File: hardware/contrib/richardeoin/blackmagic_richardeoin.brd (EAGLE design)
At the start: 5 parts, among them Q2 IRLML5103

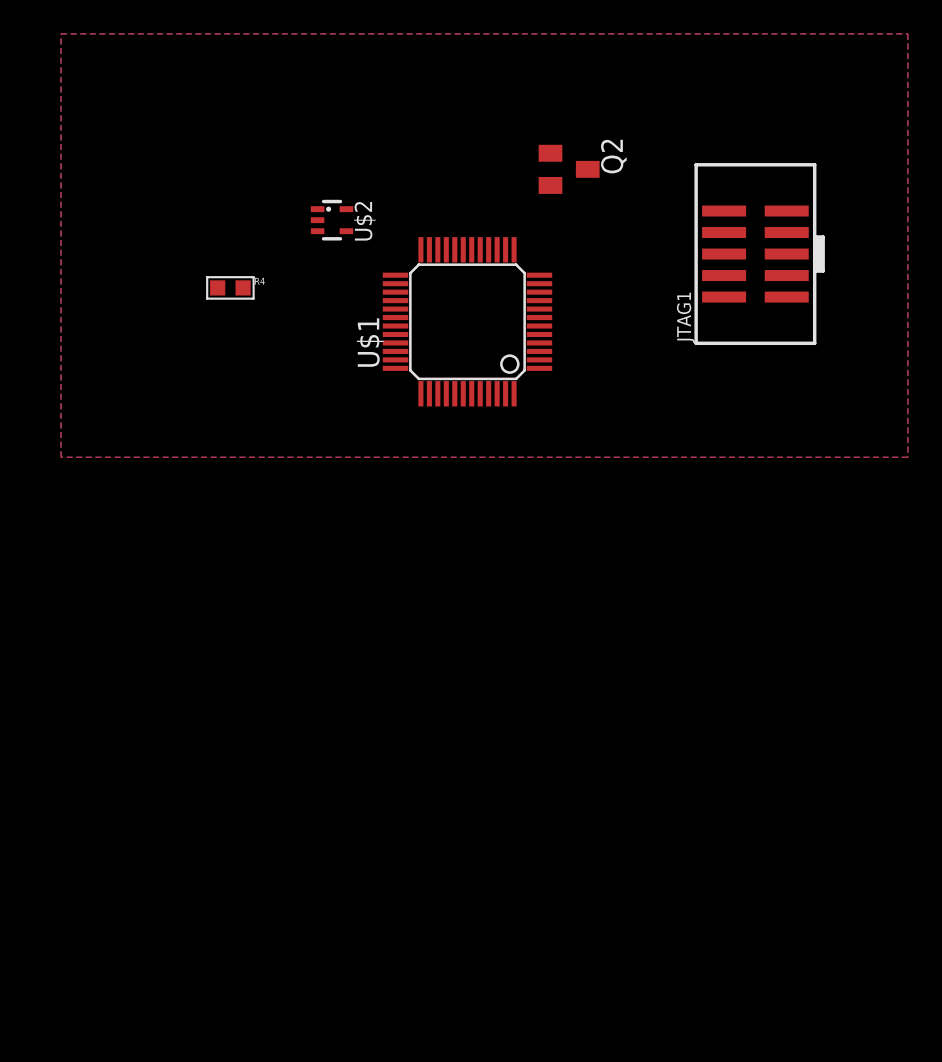
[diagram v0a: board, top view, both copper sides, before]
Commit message: Majority of Components in place
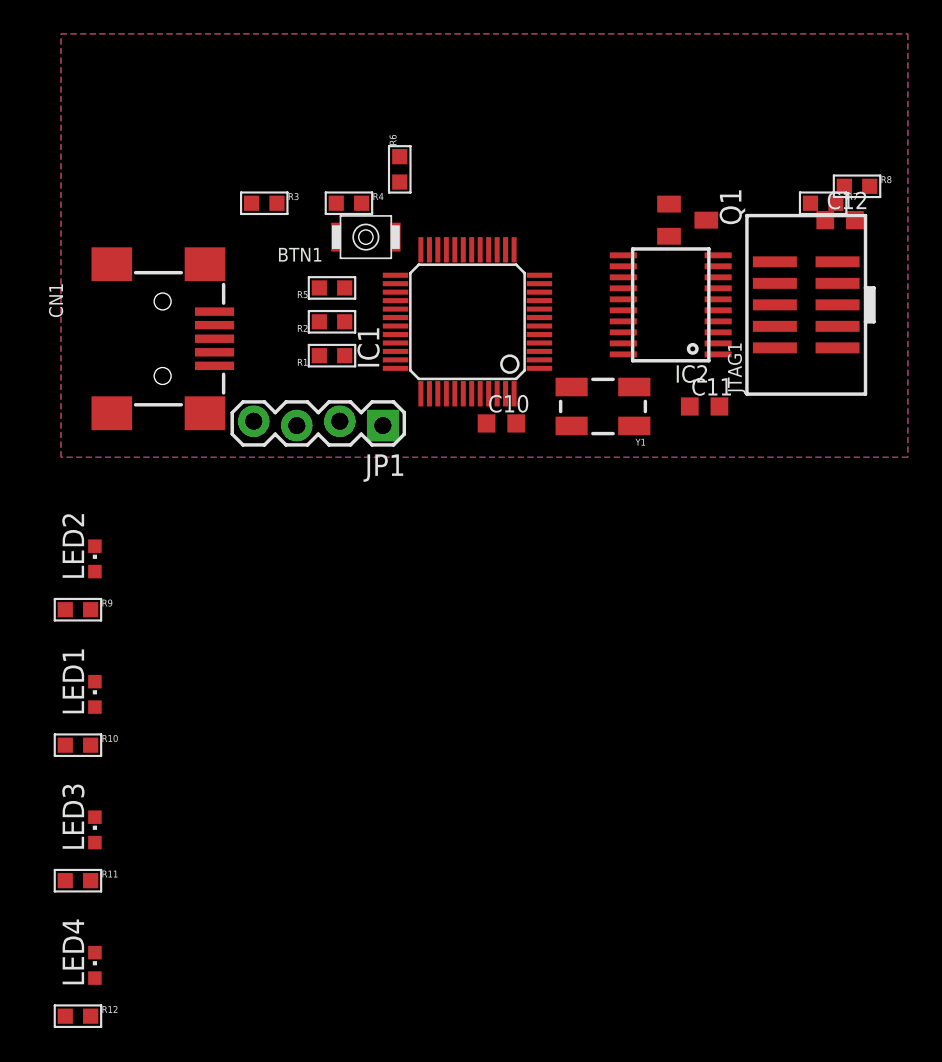
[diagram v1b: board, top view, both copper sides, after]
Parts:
- removed Q2: IRLML5103, transistor-small-signal:SOT23
- removed U$2: TLV70033DCK, tlv700:SC70-5L
- added BTN1: SPST.B3U-1000P(M)-B, omron:B3U-1000P(M)-B
- added C10, C11: 18pF, resistor:C0603K
- added C12: 100nF, resistor:C0603K
- added CN1: (no value), microbuilder_v3:USB-MINIB
- added IC2: TXS0108, dan-translate:TSSOP20
- added JP1: (no value), SparkFun:1X04_LOCK
- added LED1, LED2, LED3, LED4: (no value), led:CHIPLED_0603
- added Q1: IRLML5103, transistor-small-signal:SOT23
- added R1, R2: 22Ω, microbuilder:0603-MINI
- added R10, R11, R12, R9: 390Ω, microbuilder:0603-MINI
- added R3, R8: 4K7, microbuilder:0603-MINI
- added R5: 1K5, microbuilder:0603-MINI
- added R6, R7: 10K, microbuilder:0603-MINI
- added Y1: 12MHz, SparkFun:CRYSTAL-SMD-5X3
- moved R4 8.60 mm to (17.0, 15.0)
- moved JTAG1 4.24 mm to (44.0, 9.00)
- renumbered U$1 to IC1
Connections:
- removed net +5V: U$2.1, U$2.3
- removed net OSC_OUT: IC1.6
- new net 3.3V: IC1.1, IC1.24, IC1.36, IC1.40, IC1.41, IC1.48, IC1.9, IC2.19, JP1.1, Q1.2, R6.2
- new net 5.0V: CN1.VBUS, R3.2
- new net D+: CN1.D+, R1.2, R5.2
- new net D-: CN1.D-, R2.2
- new net FORCE_BOOTLOADER: BTN1.1, IC1.25, R6.1
- new net LPC_XTAL2: C11.2, IC1.6, Y1.1
- new net N$3: LED1.C
- new net N$6: LED3.A, R11.2
- new net N$7: LED4.C
- new net N$8: LED4.A, R12.2
- new net TARGET_POWER_ADC: C12.1, IC1.18, R7.2, R8.1
- new net TARGET_RST: IC2.8, JTAG1.10
- new net TARGET_TCK: IC2.5, JTAG1.4
- new net TARGET_TDI: IC2.7, JTAG1.8
- new net TARGET_TDO: IC2.6, JTAG1.6
- new net TARGET_TMS: IC2.4, JTAG1.2
- new net VBUS: IC1.26, R3.1, R4.2
- net GND: now also BTN1.2, C10.1, C11.1, C12.2, CN1.GND, CN1.ID, IC1.44, IC2.11, IC2.12, IC2.18, IC2.20, JP1.4, R4.1, R7.1
- net N$1: now also LED2.C; no longer Q2.2
- net N$2: now also LED2.A, R9.2; no longer U$2.5
- net N$4: now also LED1.A, R10.2; no longer IC1.1, IC1.24, IC1.36, IC1.48, IC1.9
- net N$5: now also LED3.C; no longer IC1.40, IC1.41
- net OSC_IN: now also C10.2, Y1.3
- net PWR_BR: now also Q1.1; no longer Q2.1
- net RST: now also IC2.13; no longer JTAG1.10
- net RXD: now also JP1.3
- net TCK: now also IC2.16; no longer JTAG1.4
- net TDI: now also IC2.14; no longer JTAG1.8
- net TDO: now also IC2.15; no longer JTAG1.6
- net TMS: now also IC2.17; no longer JTAG1.2
- net TPWR: now also IC2.10, IC2.2, JTAG1.1, Q1.3, R8.2; no longer Q2.3
- net TXD: now also JP1.2
- net USB_DM: now also R2.1
- net USB_DP: now also R1.1
- net USB_ENUMERATE: now also R5.1

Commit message: Added LEDs
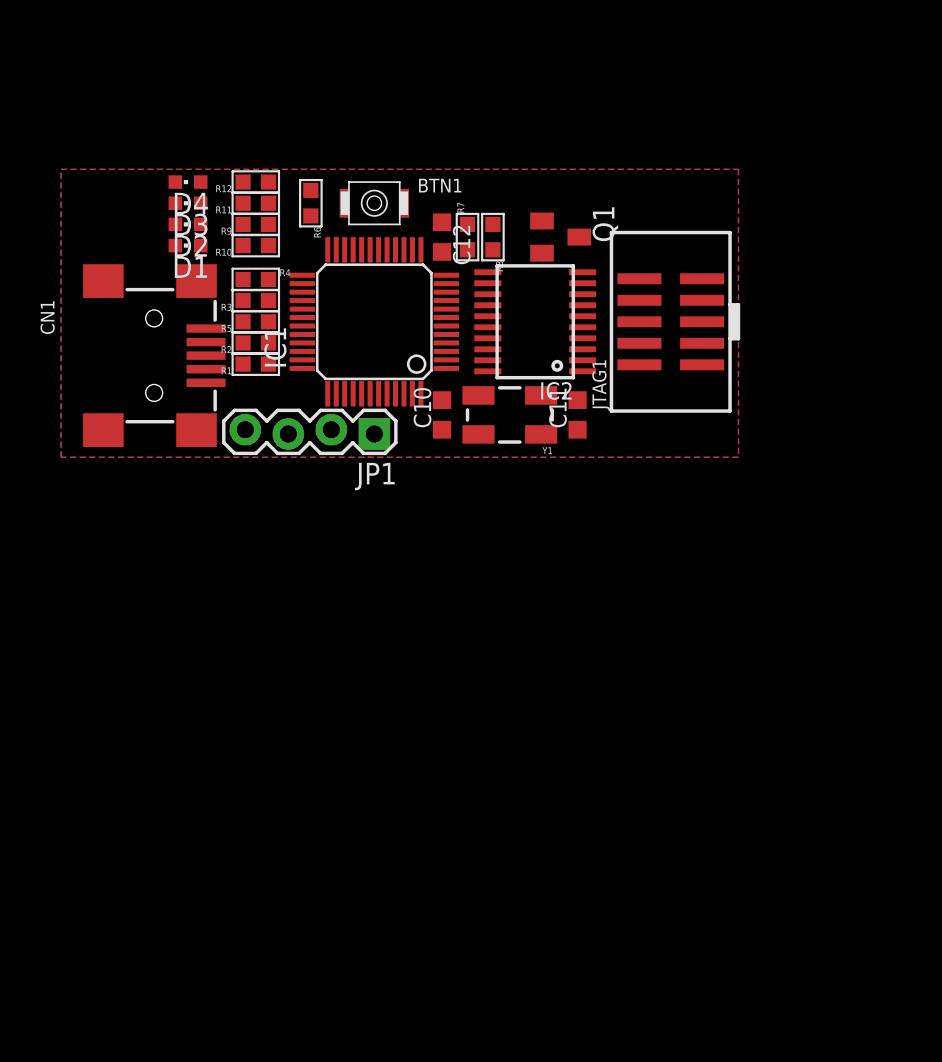
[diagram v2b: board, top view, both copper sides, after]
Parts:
- removed LED1, LED2, LED3, LED4: (no value), led:CHIPLED_0603
- added D1: GREEN, led:CHIPLED_0603
- added D2: RED, led:CHIPLED_0603
- added D3, D4: YELLOW, led:CHIPLED_0603
- Y1: value 12MHz -> 8MHz
- moved R12 50.4 mm to (11.5, 16.2), turned to 180 degrees
- moved R11 41.4 mm to (11.5, 15.0), turned to 180 degrees
- moved R10 31.3 mm to (11.5, 12.5), turned to 180 degrees
- moved R9 25.1 mm to (11.5, 13.8), turned to 180 degrees
- moved C12 23.5 mm to (22.5, 13.0), turned to 270 degrees
- moved R8 21.7 mm to (25.5, 13.0), turned to 270 degrees
- moved R7 21.1 mm to (24.0, 13.0), turned to 90 degrees
- moved IC2 8.06 mm to (28.0, 8.00)
- moved JTAG1 8.06 mm to (36.0, 8.00)
- moved Q1 7.57 mm to (29.5, 13.0)
- moved C11 7.52 mm to (30.5, 2.50), turned to 90 degrees
- moved R4 7.11 mm to (11.5, 10.5)
- moved R3 5.77 mm to (11.5, 9.25), turned to 180 degrees
- moved R6 5.62 mm to (14.8, 15.0), turned to 270 degrees
- moved Y1 5.52 mm to (26.5, 2.50)
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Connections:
- removed net N$1: LED2.C
- removed net N$3: LED1.C
- removed net N$5: LED3.C
- removed net N$7: LED4.C
- net 3.3V: now also R10.1
- net GND: now also D1.C, D2.C, D3.C, D4.C
- net LED0: now also R12.1
- net LED1: now also R11.1
- net LED2: now also R9.1
- net N$2: now also D2.A; no longer LED2.A
- net N$4: now also D1.A; no longer LED1.A
- net N$6: now also D3.A; no longer LED3.A
- net N$8: now also D4.A; no longer LED4.A

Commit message: Schematic provisionally complete
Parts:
- added C1, C2: 1µF, resistor:C0603K
- added C3, C4, C5: 100nF, resistor:C0603K
- added U$21: TLV70033DCK, tlv700:SC70-5L
- moved BTN1 9.10 mm to (9.75, 12.5), turned to 180 degrees
- moved R10 6.33 mm to (5.25, 11.5)
- moved R11 6.33 mm to (5.25, 14.0)
- moved R12 6.33 mm to (5.25, 15.2)
- moved R9 6.33 mm to (5.25, 12.8)
- moved D4 6.08 mm to (1.50, 15.2)
- moved D3 6.05 mm to (1.50, 14.2)
- moved D2 6.02 mm to (1.50, 13.2)
- moved D1 6.01 mm to (1.50, 12.2)
- moved R6 2.69 mm to (13.8, 12.5), turned to 0 degrees
- moved C10 2.00 mm to (24.5, 2.50)
- moved Y1 1.50 mm to (28.0, 2.50)
- moved C11 1.00 mm to (31.5, 2.50)
- moved IC2 1.00 mm to (29.0, 8.00)
- moved CN1 0.50 mm to (4.50, 5.50)
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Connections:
- net 3.3V: now also C2.1, C3.1, C4.1, C5.1, U$21.5
- net 5.0V: now also C1.1, U$21.1, U$21.3
- net GND: now also C1.2, C2.2, C3.2, C4.2, C5.2, U$21.2

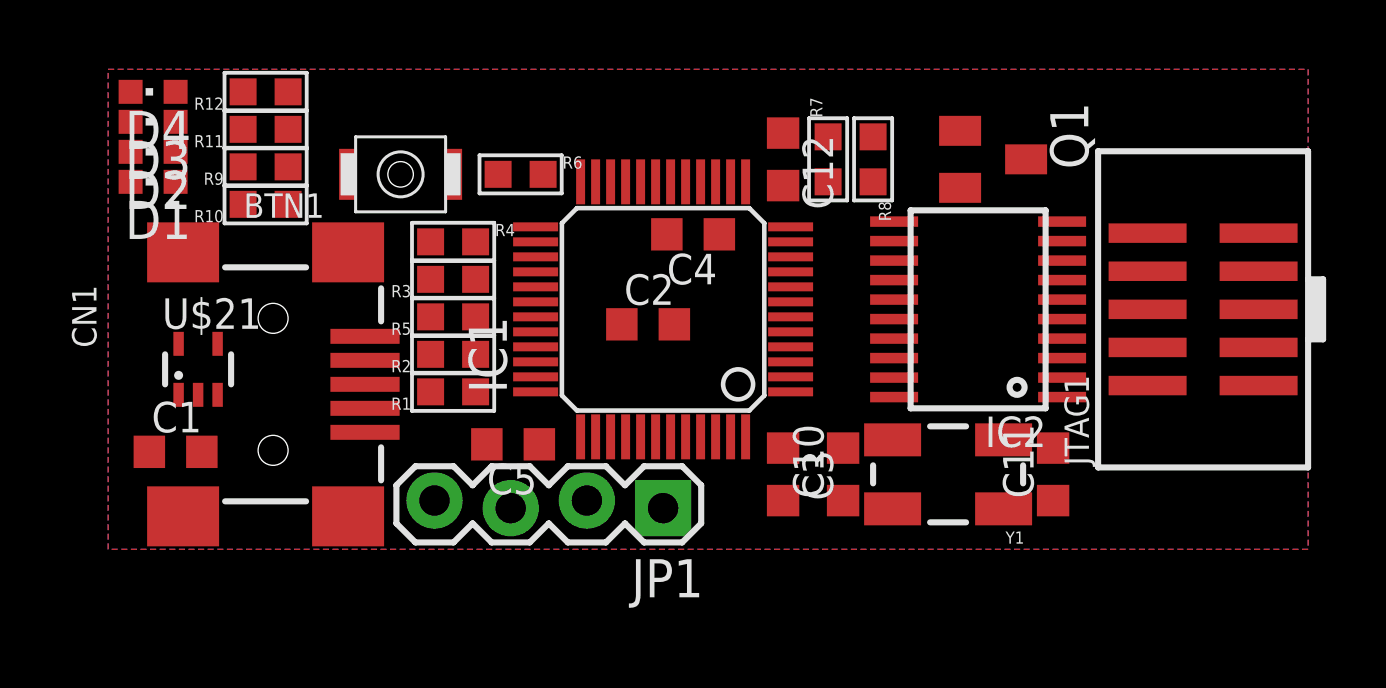
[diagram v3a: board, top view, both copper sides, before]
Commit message: Completed board layout
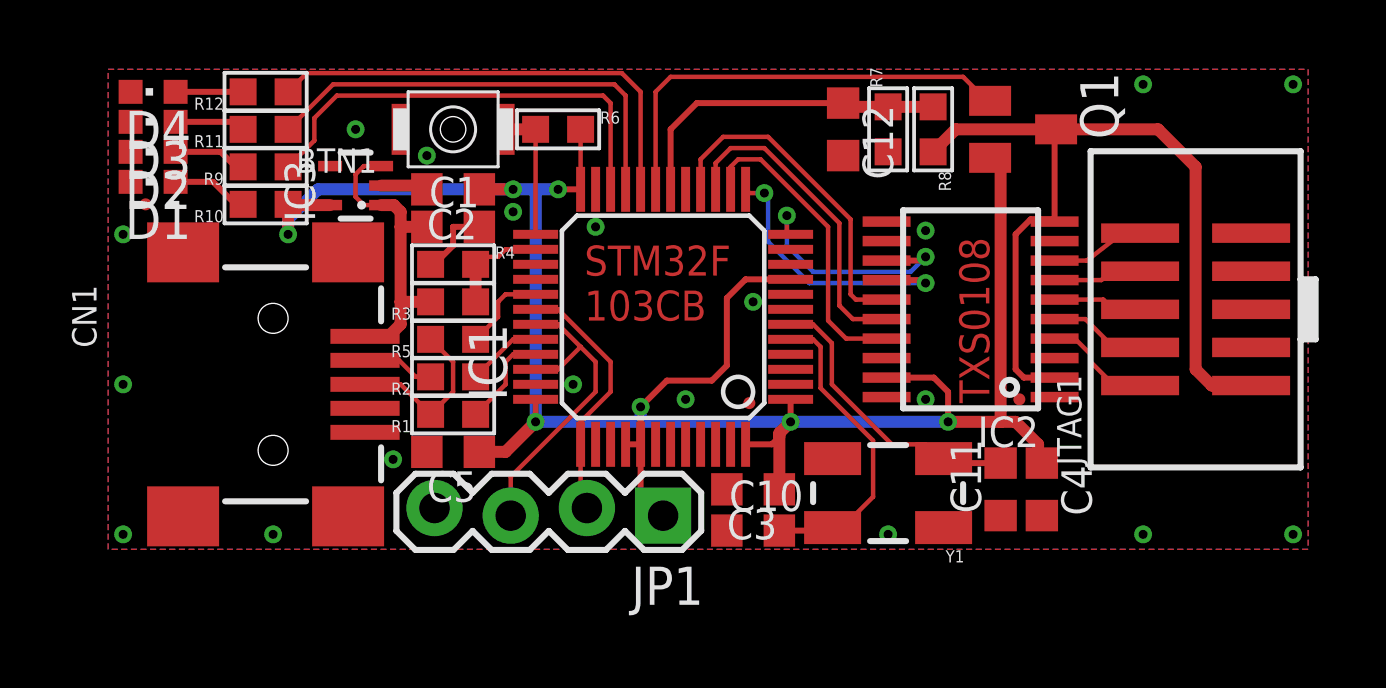
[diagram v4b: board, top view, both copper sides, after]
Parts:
- removed U$21: TLV70033DCK, tlv700:SC70-5L
- added IC3: TLV70033DCK, tlv700:SC70-5L
- moved C4 14.4 mm to (31.1, 2.00), turned to 270 degrees
- moved C1 11.9 mm to (11.5, 10.8)
- moved C2 7.91 mm to (11.5, 12.0), turned to 180 degrees
- moved C10 3.54 mm to (21.5, 0.62), turned to 0 degrees
- moved BTN1 2.30 mm to (11.5, 14.0)
- moved C12 2.24 mm to (24.5, 14.0)
- moved R7 2.24 mm to (26.0, 14.0)
- moved R8 2.24 mm to (27.5, 14.0)
- moved Y1 2.10 mm to (26.0, 1.88)
- moved C5 2.02 mm to (11.5, 3.25)
- moved R6 1.95 mm to (15.0, 14.0)
- moved C11 1.82 mm to (29.8, 2.00)
- moved Q1 1.41 mm to (30.5, 14.0)
- moved C3 1.12 mm to (21.5, 2.00), turned to 180 degrees
- moved R1 0.75 mm to (11.5, 4.50)
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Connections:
- net 3.3V: now also IC3.5; no longer U$21.5
- net 5.0V: now also IC3.1, IC3.3; no longer U$21.1, U$21.3
- net GND: now also IC3.2; no longer U$21.2
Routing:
- net 3.3V: track 0.00 -> 74.3 mm, vias 0 -> 7
- net TPWR: track 0.00 -> 28.9 mm
- net LED0: track 0.00 -> 15.5 mm
- net LED2: track 0.00 -> 15.2 mm
- net LED1: track 0.00 -> 15.2 mm
- net PWR_BR: track 0.00 -> 14.9 mm
- net TDO: track 0.00 -> 11.2 mm
- net TARGET_POWER_ADC: track 0.00 -> 11.2 mm
- net TCK: track 0.00 -> 10.8 mm
- net RXD: track 0.00 -> 10.6 mm
- net 5.0V: track 0.00 -> 10.4 mm
- net OSC_IN: track 0.00 -> 10.4 mm
- net TMS: track 0.00 -> 10.4 mm
- net LPC_XTAL2: track 0.00 -> 9.70 mm
- net TDI: track 0.00 -> 9.51 mm, vias 0 -> 2
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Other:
- board text added: "STM32F 103CB"
- board text added: "TXS0108"

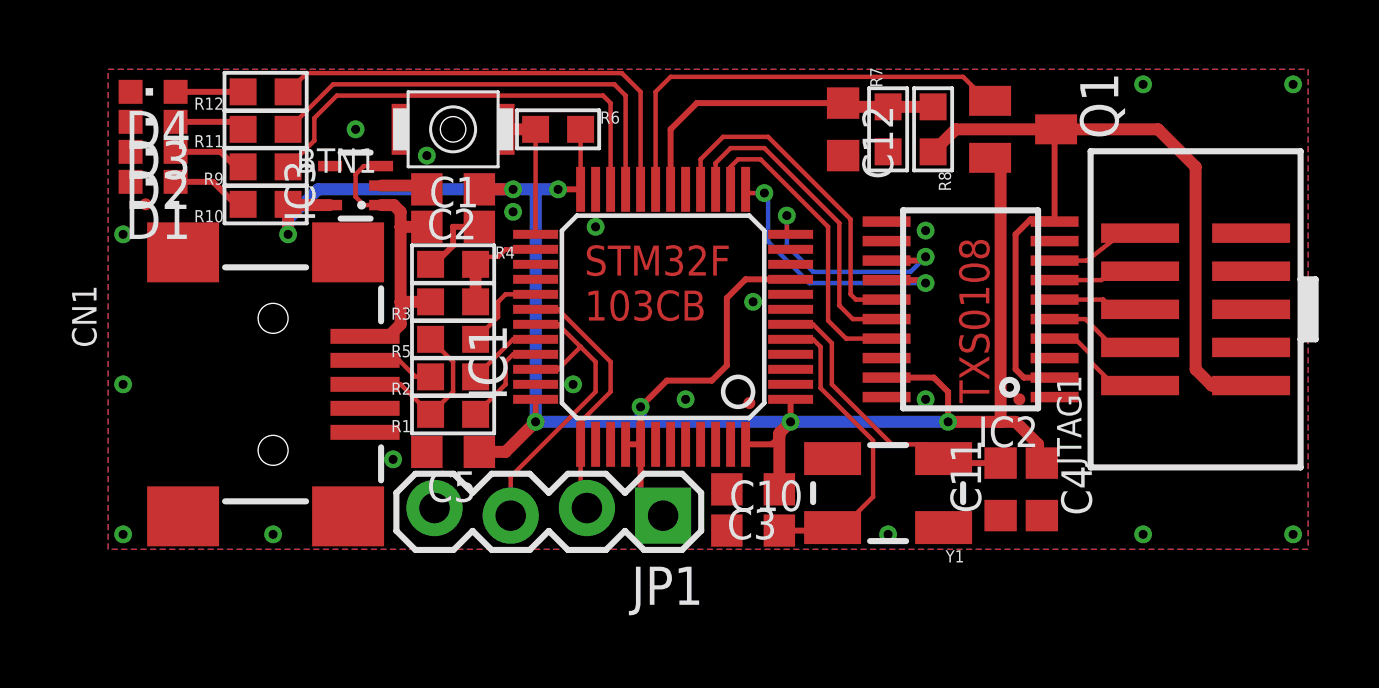
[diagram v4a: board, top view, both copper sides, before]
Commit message: Changed text on the end of the board to "ARM Cortex Debug"
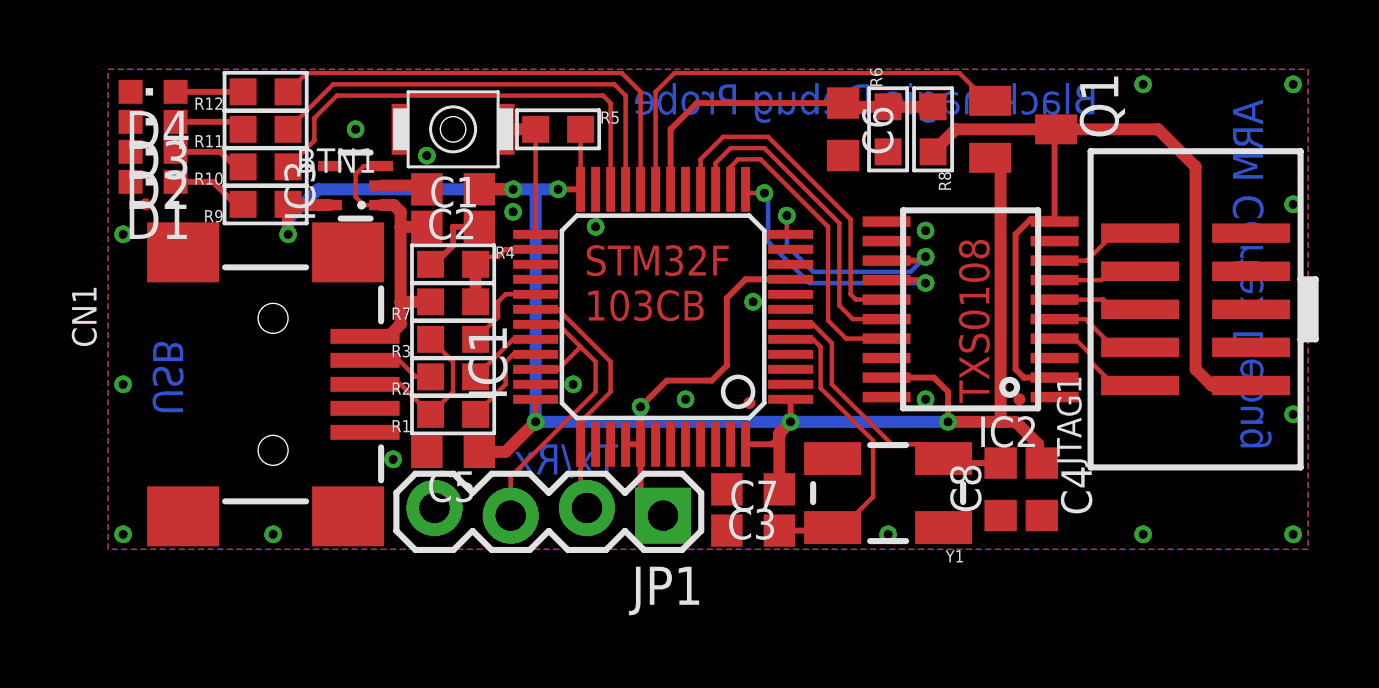
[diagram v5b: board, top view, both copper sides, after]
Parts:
- R3: value 4K7 -> 1K5
- R5: value 1K5 -> 10K
- R7: value 10K -> 4K7
- moved R7 15.6 mm to (11.5, 8.25), turned to 180 degrees
- moved R6 11.0 mm to (26.0, 14.0), turned to 90 degrees
- moved R5 7.83 mm to (15.0, 14.0), turned to 0 degrees
- moved R10 1.25 mm to (5.25, 12.8)
- moved R3 1.25 mm to (11.5, 7.00)
- moved R9 1.25 mm to (5.25, 11.5)
- renumbered C10 to C7, C11 to C8, C12 to C6
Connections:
- net 3.3V: now also R5.2, R9.1; no longer R10.1, R6.2
- net 5.0V: now also R7.2; no longer R3.2
- net D+: now also R3.2; no longer R5.2
- net FORCE_BOOTLOADER: now also R5.1; no longer R6.1
- net GND: now also R6.1; no longer R7.1
- net LED2: now also R10.1; no longer R9.1
- net N$2: now also R10.2; no longer R9.2
- net N$4: now also R9.2; no longer R10.2
- net TARGET_POWER_ADC: now also R6.2; no longer R7.2
- net USB_ENUMERATE: now also R3.1; no longer R5.1
- net VBUS: now also R7.1; no longer R3.1
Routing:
- net KEY: track 0.00 -> 2.00 mm
- net GND: vias 19 -> 21
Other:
- board text added: "ARM Cortex Debug"
- board text added: "Blackmagic Debug Probe"
- board text added: "Tx/Rx"
- board text added: "USB"
